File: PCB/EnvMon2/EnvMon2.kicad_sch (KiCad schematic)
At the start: 38 parts, among them J1 USB-C, J2 DC, J3 TEMP, J4 Shelly, M1 OLED1.5-RGB, SW1 SW_Push, SW2 SW_Push, SW3 SW_Push, U1 LMR16006XDDCR, U2 SCD41, U3 FT231XQ, U4 ESP32-PICO-MINI-02, U5 QR, U6 VEML3235SL_RA

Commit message: Tweak connectors
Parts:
- J2: footprint RevK:Molex_MiniSPOX_H2RA -> RevK:PTSM-HH-2-RA-W; Notes Not fitted -> (none)
- J3: footprint RevK:Molex_MiniSPOX_H3RA -> RevK:PTSM-HH-3-RA
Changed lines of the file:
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@@
       (effects (font (size 1.27 1.27)) (justify right))
     )
-    (property "Footprint" "RevK:Molex_MiniSPOX_H2RA" (id 2) (at 53.34 121.285 0)
+    (property "Footprint" "RevK:PTSM-HH-2-RA-W" (id 2) (at 53.34 121.285 0)
       (effects (font (size 1.27 1.27)) hide)
     )
     (property "Datasheet" "~" (id 3) (at 53.34 121.285 0)
-      (effects (font (size 1.27 1.27)) hide)
-    )
-    (property "Notes" "Not fitted" (id 4) (at 53.34 121.285 0)
       (effects (font (size 1.27 1.27)) hide)
     )
@@
       (effects (font (size 1.27 1.27)) (justify left))
     )
-    (property "Footprint" "RevK:Molex_MiniSPOX_H3RA" (id 2) (at 203.2 134.62 0)
+    (property "Footprint" "RevK:PTSM-HH-3-RA" (id 2) (at 203.2 134.62 0)
       (effects (font (size 1.27 1.27)) hide)
     )
@@
     )
     (path "/05c95e20-b8ce-45a0-abe6-40ea1ba1906f"
-      (reference "J2") (unit 1) (value "DC") (footprint "RevK:Molex_MiniSPOX_H2RA")
+      (reference "J2") (unit 1) (value "DC") (footprint "RevK:PTSM-HH-2-RA-W")
     )
     (path "/3831277e-1b7d-4fa1-a209-da364bd7b5c6"
-      (reference "J3") (unit 1) (value "TEMP") (footprint "RevK:Molex_MiniSPOX_H3RA")
+      (reference "J3") (unit 1) (value "TEMP") (footprint "RevK:PTSM-HH-3-RA")
     )
     (path "/10964051-8ae1-4f03-bdfe-2aa594809f6d"

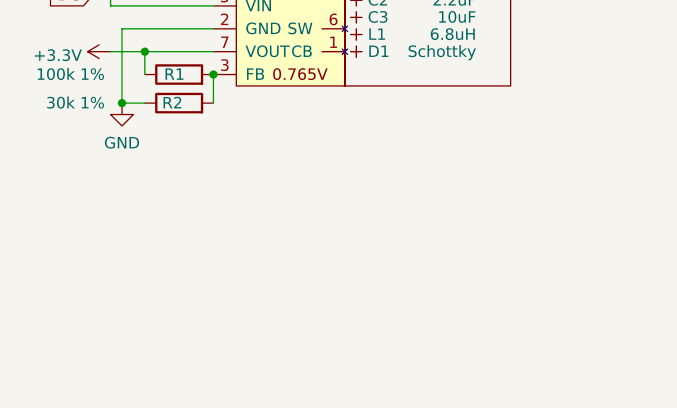
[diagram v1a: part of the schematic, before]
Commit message: New PCB with Sensitron SHT40 on board
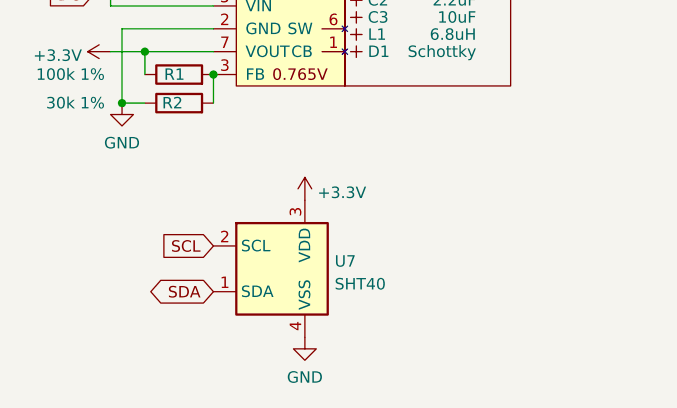
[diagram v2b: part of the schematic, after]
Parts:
- added U7: SHT40, RevK:Sensirion_DFN-4_1.5x1.5mm_P0.5mm_SHT4x, symbol RevK:SHT40
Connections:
- net +3.3V: now also U7.3 (VDD)
- net GND: now also U7.4 (VSS)
- net SCL: now also U7.2 (SCL)
- net SDA: now also U7.1 (SDA)
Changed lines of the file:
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@@
+    )
+  )
+  (global_label "SCL" (shape input) (at 49.53 161.29 180) (fields_autoplaced)
+    (effects (font (size 1.27 1.27)) (justify right))
+    (property "Intersheet References" "${INTERSHEET_REFS}" (id 0) (at 43.6982 161.2106 0)
+      (effects (font (size 1.27 1.27)) (justify right) hide)
     )
   )
@@
     (effects (font (size 1.27 1.27)) (justify right))
     (property "Intersheet References" "${INTERSHEET_REFS}" (id 0) (at 185.8777 124.3806 0)
+      (effects (font (size 1.27 1.27)) (justify right) hide)
+    )
+  )
+  (global_label "SDA" (shape bidirectional) (at 49.53 166.37 180) (fields_autoplaced)
+    (effects (font (size 1.27 1.27)) (justify right))
+    (property "Intersheet References" "${INTERSHEET_REFS}" (id 0) (at 43.6377 166.2906 0)
       (effects (font (size 1.27 1.27)) (justify right) hide)
     )
@@
     (pin "5")
   )
+  (symbol (lib_id "power:+3.3V") (at 59.69 156.21 0) (unit 1)
+    (in_bom yes) (on_board yes) (fields_autoplaced)
+    (property "Reference" "#PWR?" (id 0) (at 59.69 160.02 0)
+      (effects (font (size 1.27 1.27)) hide)
+    )
+    (property "Value" "+3.3V" (id 1) (at 61.087 155.3738 0)
+      (effects (font (size 1.27 1.27)) (justify left))
+    )
+    (property "Footprint" "" (id 2) (at 59.69 156.21 0)
+      (effects (font (size 1.27 1.27)) hide)
+    )
+    (property "Datasheet" "" (id 3) (at 59.69 156.21 0)
+      (effects (font (size 1.27 1.27)) hide)
+    )
+    (pin "1")
+  )
   (symbol (lib_id "power:GND") (at 198.12 132.08 270) (unit 1)
     (in_bom yes) (on_board yes) (fields_autoplaced)
@@
     )
     (pin "~")
+  )
+  (symbol (lib_id "power:GND") (at 59.69 171.45 0) (unit 1)
+    (in_bom yes) (on_board yes) (fields_autoplaced)
+    (property "Reference" "#PWR?" (id 0) (at 59.69 177.8 0)
+      (effects (font (size 1.27 1.27)) hide)
+    )
+    (property "Value" "GND" (id 1) (at 59.69 175.8934 0))
+    (property "Footprint" "" (id 2) (at 59.69 171.45 0)
+      (effects (font (size 1.27 1.27)) hide)
+    )
+    (property "Datasheet" "" (id 3) (at 59.69 171.45 0)
+      (effects (font (size 1.27 1.27)) hide)
+    )
+    (pin "1")
   )
   (symbol (lib_id "Device:R") (at 62.23 45.72 90) (unit 1)
@@
     (pin "4")
   )
+  (symbol (lib_id "RevK:SHT40") (at 57.15 163.83 0) (unit 1)
+    (in_bom yes) (on_board yes) (fields_autoplaced)
+    (property "Reference" "U7" (id 0) (at 62.992 162.9953 0)
+      (effects (font (size 1.27 1.27)) (justify left))
+    )
+    (property "Value" "SHT40" (id 1) (at 62.992 165.5322 0)
+      (effects (font (size 1.27 1.27)) (justify left))
+    )
+    (property "Footprint" "RevK:Sensirion_DFN-4_1.5x1.5mm_P0.5mm_SHT4x" (id 2) (at 60.96 170.18 0)
+      (effects (font (size 1.27 1.27)) (justify left) hide)
+    )
+    (property "Datasheet" "https://sensirion.com/media/documents/33FD6951/624C4357/Datasheet_SHT4x.pdf" (id 3) (at 60.96 172.72 0)
+      (effects (font (size 1.27 1.27)) (justify left) hide)
+    )
+    (property "LCSC Part #" "C2909890" (id 4) (at 62.992 166.8007 0)
+      (effects (font (size 1.27 1.27)) (justify left) hide)
+    )
+    (pin "1")
+    (pin "2")
+    (pin "3")
+    (pin "4")
+  )
   (symbol (lib_id "power:+3.3V") (at 229.235 46.99 270) (unit 1)
     (in_bom yes) (on_board yes) (fields_autoplaced)
@@
       (reference "#PWR0109") (unit 1) (value "+3.3V") (footprint "")
     )
+    (path "/129f3b96-7fb3-4974-a9d3-a0445557145a"
+      (reference "#PWR?") (unit 1) (value "+3.3V") (footprint "")
+    )
+    (path "/6431a231-0120-45c3-a65d-98ba98211f0a"
+      (reference "#PWR?") (unit 1) (value "GND") (footprint "")
+    )
     (path "/55f1b135-41b1-4a91-addc-adbe226d5adc"
       (reference "C1") (unit 1) (value "100nF") (footprint "RevK:C_0603_")
@@
       (reference "U6") (unit 1) (value "VEML3235SL_RA") (footprint "RevK:VEML3235SL-RA")
     )
-  )
+    (path "/c7273ae8-7990-45e3-8b03-3202e8645907"
+      (reference "U7") (unit 1) (value "SHT40") (footprint "RevK:Sensirion_DFN-4_1.5x1.5mm_P0.5mm_SHT4x")
+    )
+  )

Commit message: Started EnvHT
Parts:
- added C5: 100nF, RevK:C_0603, symbol Device:C
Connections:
- net +3.3V: now also C5.1
- net GND: now also C5.2
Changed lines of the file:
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@@
   (junction (at 226.06 44.45) (diameter 0) (color 0 0 0 0)
   )
+  (junction (at 59.69 156.21) (diameter 0) (color 0 0 0 0)
+  )
   (junction (at 66.04 33.02) (diameter 0) (color 0 0 0 0)
+  )
+  (junction (at 59.69 171.45) (diameter 0) (color 0 0 0 0)
   )
   (junction (at 40.64 66.04) (diameter 0) (color 0 0 0 0)
@@
     (stroke (width 0) (type default) (color 0 0 0 0))
   )
+  (wire (pts (xy 72.39 156.21) (xy 59.69 156.21))
+    (stroke (width 0) (type default) (color 0 0 0 0))
+  )
   (wire (pts (xy 36.195 133.35) (xy 38.1 133.35))
     (stroke (width 0) (type default) (color 0 0 0 0))
@@
     (stroke (width 0) (type default) (color 0 0 0 0))
   )
+  (wire (pts (xy 72.39 171.45) (xy 59.69 171.45))
+    (stroke (width 0) (type default) (color 0 0 0 0))
+  )
   (wire (pts (xy 66.04 107.95) (xy 68.58 107.95))
     (stroke (width 0) (type default) (color 0 0 0 0))
@@
     (stroke (width 0) (type default) (color 0 0 0 0))
   )
+  (wire (pts (xy 72.39 160.02) (xy 72.39 156.21))
+    (stroke (width 0) (type default) (color 0 0 0 0))
+  )
   (wire (pts (xy 38.1 133.35) (xy 38.1 134.62))
     (stroke (width 0) (type default) (color 0 0 0 0))
@@
   )
   (wire (pts (xy 132.08 66.04) (xy 134.62 66.04))
+    (stroke (width 0) (type default) (color 0 0 0 0))
+  )
+  (wire (pts (xy 72.39 167.64) (xy 72.39 171.45))
     (stroke (width 0) (type default) (color 0 0 0 0))
   )
@@
   (symbol (lib_id "power:+3.3V") (at 59.69 156.21 0) (unit 1)
     (in_bom yes) (on_board yes) (fields_autoplaced)
-    (property "Reference" "#PWR?" (id 0) (at 59.69 160.02 0)
+    (property "Reference" "#PWR0111" (id 0) (at 59.69 160.02 0)
       (effects (font (size 1.27 1.27)) hide)
     )
@@
     )
     (pin "1")
+  )
+  (symbol (lib_id "Device:C") (at 72.39 163.83 0) (unit 1)
+    (in_bom yes) (on_board yes) (fields_autoplaced)
+    (property "Reference" "C5" (id 0) (at 75.311 162.9953 0)
+      (effects (font (size 1.27 1.27)) (justify left))
+    )
+    (property "Value" "100nF" (id 1) (at 75.311 165.5322 0)
+      (effects (font (size 1.27 1.27)) (justify left))
+    )
+    (property "Footprint" "RevK:C_0603" (id 2) (at 73.3552 167.64 0)
+      (effects (font (size 1.27 1.27)) hide)
+    )
+    (property "Datasheet" "~" (id 3) (at 72.39 163.83 0)
+      (effects (font (size 1.27 1.27)) hide)
+    )
+    (pin "1")
+    (pin "2")
   )
   (symbol (lib_id "RevK:SCD41") (at 66.04 96.52 0) (unit 1)
@@
   (symbol (lib_id "power:GND") (at 59.69 171.45 0) (unit 1)
     (in_bom yes) (on_board yes) (fields_autoplaced)
-    (property "Reference" "#PWR?" (id 0) (at 59.69 177.8 0)
+    (property "Reference" "#PWR0110" (id 0) (at 59.69 177.8 0)
       (effects (font (size 1.27 1.27)) hide)
     )
@@
       (reference "#PWR0109") (unit 1) (value "+3.3V") (footprint "")
     )
+    (path "/6431a231-0120-45c3-a65d-98ba98211f0a"
+      (reference "#PWR0110") (unit 1) (value "GND") (footprint "")
+    )
     (path "/129f3b96-7fb3-4974-a9d3-a0445557145a"
-      (reference "#PWR?") (unit 1) (value "+3.3V") (footprint "")
-    )
-    (path "/6431a231-0120-45c3-a65d-98ba98211f0a"
-      (reference "#PWR?") (unit 1) (value "GND") (footprint "")
+      (reference "#PWR0111") (unit 1) (value "+3.3V") (footprint "")
     )
     (path "/55f1b135-41b1-4a91-addc-adbe226d5adc"
@@
       (reference "C4") (unit 1) (value "10nF") (footprint "RevK:C_0603")
     )
+    (path "/58daac71-ff3f-43e9-821c-80104525ed72"
+      (reference "C5") (unit 1) (value "100nF") (footprint "RevK:C_0603")
+    )
     (path "/6317ccc8-6edd-48eb-98c0-5a7f98d8bfba"

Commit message: Silk and change VEML
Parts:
- removed U6: VEML3235SL_RA, RevK:VEML3235SL-RA, symbol RevK:VEML3235SL_RA
- added U8: VEML6040, RevK:VEML6040, symbol RevK:VEML6040
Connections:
- net +3.3V: now also U8.4 (VDD)
- net GND: now also U8.1 (GND)
- net SCL: now also U8.3 (SCL)
- net SDA: now also U8.2 (SDA)
